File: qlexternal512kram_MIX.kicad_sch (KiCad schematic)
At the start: 13 parts, among them J1 QL_SLOT_DIN41612_CARD, J2 QL_SLOT_DIN41612_CARD, U1 AS6C4008-55PCN, U2 GAL16V8, U3 LM1117-5.0

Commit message: Fix reference for IC
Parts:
- U1: value AS6C4008-55PCN -> HM628512BLFP-7
- U2: value GAL16V8 -> GAL16V8B-25QP
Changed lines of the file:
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@@
     (in_bom yes) (on_board yes)
     (property "Reference" "U1" (id 0) (at 177.165 34.925 0))
-    (property "Value" "AS6C4008-55PCN" (id 1) (at 172.085 37.465 0))
+    (property "Value" "HM628512BLFP-7" (id 1) (at 172.085 37.465 0))
     (property "Footprint" "Package_SO:SSOP-32_11.305x20.495mm_P1.27mm" (id 2) (at 182.88 62.23 0)
       (effects (font (size 1.27 1.27)) hide)
@@
     (in_bom yes) (on_board yes)
     (property "Reference" "U2" (id 0) (at 241.3 106.68 0))
-    (property "Value" "GAL16V8" (id 1) (at 241.3 109.22 0))
+    (property "Value" "GAL16V8B-25QP" (id 1) (at 238.76 109.22 0))
     (property "Footprint" "Package_DIP:DIP-20_W7.62mm_LongPads" (id 2) (at 248.92 125.73 0)
       (effects (font (size 1.27 1.27)) hide)
@@
     )
     (path "/2307b488-4a2e-490d-9ec0-0a3dca2c731a"
-      (reference "U1") (unit 1) (value "AS6C4008-55PCN") (footprint "Package_SO:SSOP-32_11.305x20.495mm_P1.27mm")
+      (reference "U1") (unit 1) (value "HM628512BLFP-7") (footprint "Package_SO:SSOP-32_11.305x20.495mm_P1.27mm")
     )
     (path "/723d583a-7dea-4936-8d46-6a87035bc142"
-      (reference "U2") (unit 1) (value "GAL16V8") (footprint "Package_DIP:DIP-20_W7.62mm_LongPads")
+      (reference "U2") (unit 1) (value "GAL16V8B-25QP") (footprint "Package_DIP:DIP-20_W7.62mm_LongPads")
     )
     (path "/5ac2c658-ce29-46fb-894d-f99c774c93d1"

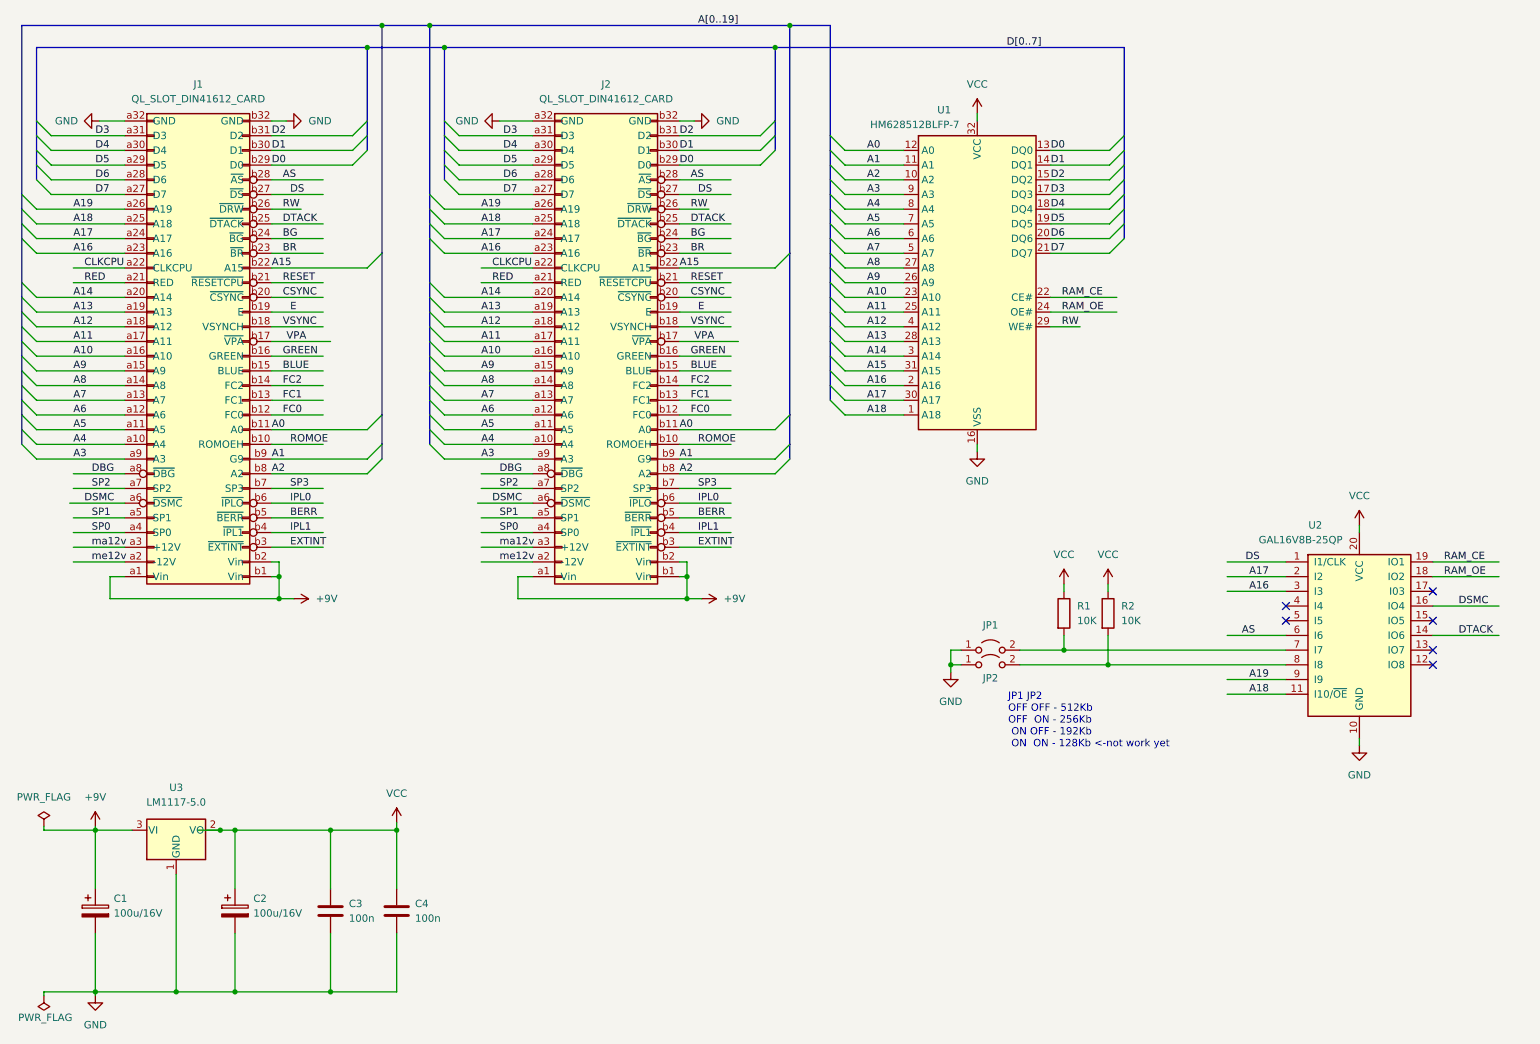
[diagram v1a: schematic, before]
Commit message: Update QL Conector
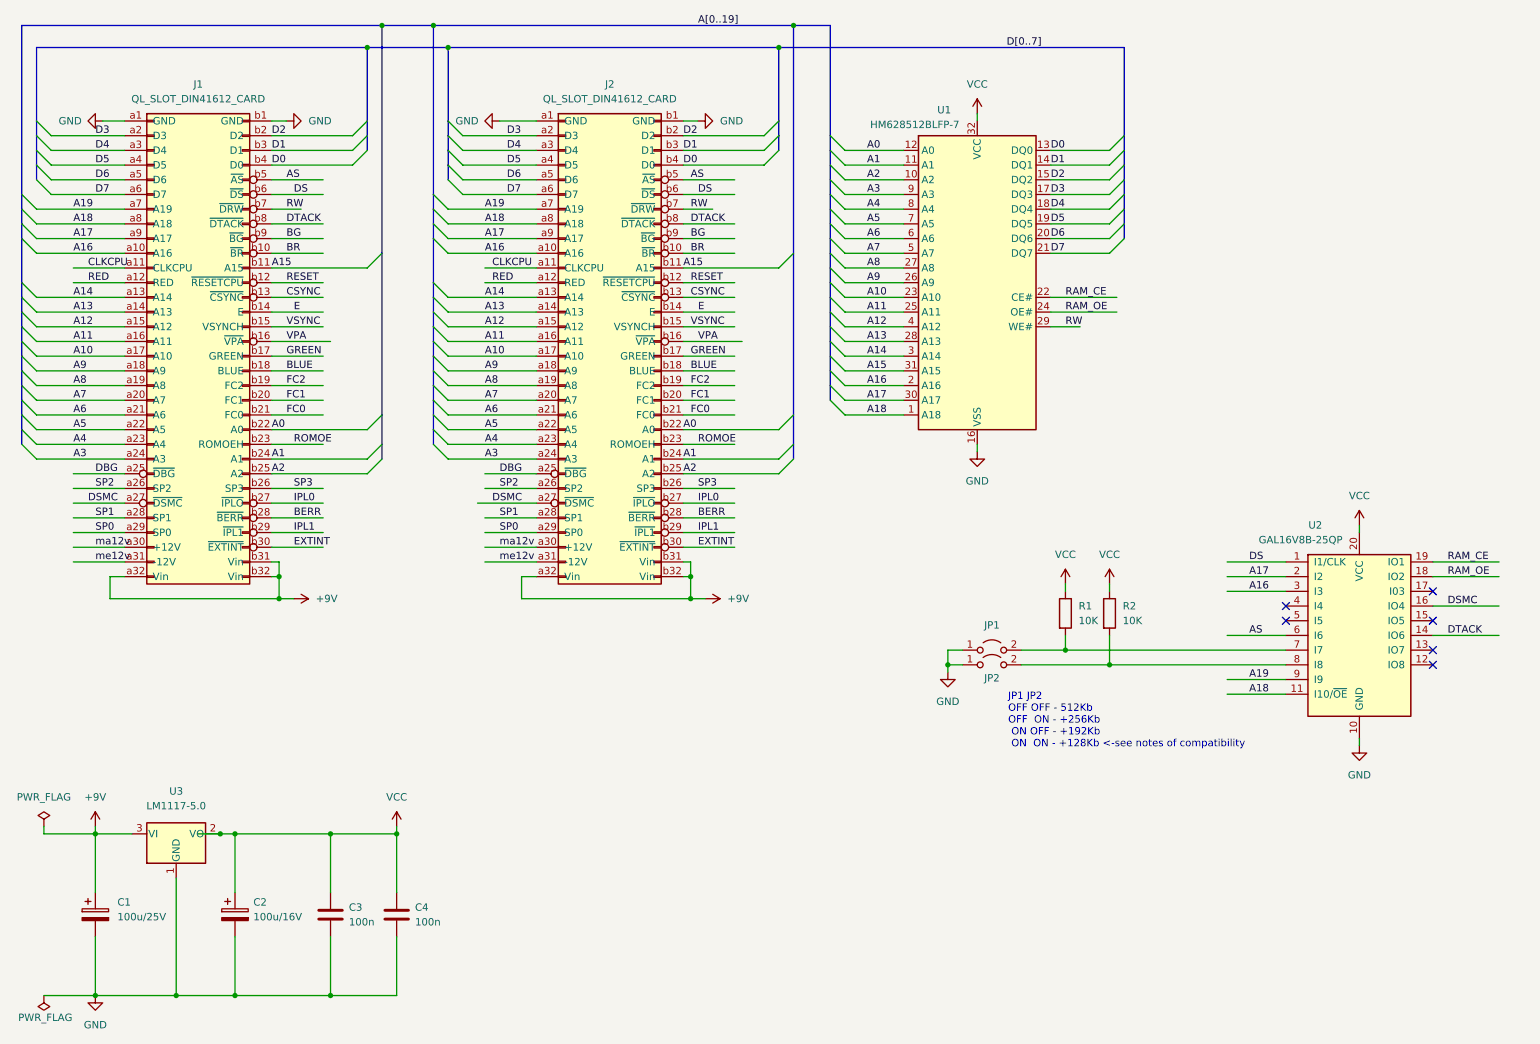
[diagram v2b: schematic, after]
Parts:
- C1: value 100u/16V -> 100u/25V
- J1, J2: symbol 8bits:QL_SLOT_DIN41612_CARD -> 8bits:QL_SLOT_DIN41612
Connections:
- net +9V: now also J1.a32 (Vin), J1.b31 (Vin), J1.b32 (Vin), J2.a32 (Vin), J2.b31 (Vin), J2.b32 (Vin); no longer J1.a1 (Vin), J1.b1 (Vin), J1.b2 (Vin), J2.a1 (Vin), J2.b1 (Vin), J2.b2 (Vin)
- net A0: now also J1.b22 (A0), J2.b22 (A0); no longer J1.b11 (A0), J2.b11 (A0)
- net A1: now also J1.b24 (A1), J2.b24 (A1); no longer J1.b9 (G9), J2.b9 (G9)
- net A10: now also J1.a17 (A10), J2.a17 (A10); no longer J1.a16 (A10), J2.a16 (A10)
- net A11: now also J1.a16 (A11), J2.a16 (A11); no longer J1.a17 (A11), J2.a17 (A11)
- net A12: now also J1.a15 (A12), J2.a15 (A12); no longer J1.a18 (A12), J2.a18 (A12)
- net A13: now also J1.a14 (A13), J2.a14 (A13); no longer J1.a19 (A13), J2.a19 (A13)
- net A14: now also J1.a13 (A14), J2.a13 (A14); no longer J1.a20 (A14), J2.a20 (A14)
- net A15: now also J1.b11 (A15), J2.b11 (A15); no longer J1.b22 (A15), J2.b22 (A15)
- net A16: now also J1.a10 (A16), J2.a10 (A16); no longer J1.a23 (A16), J2.a23 (A16)
- net A17: now also J1.a9 (A17), J2.a9 (A17); no longer J1.a24 (A17), J2.a24 (A17)
- net A18: now also J1.a8 (A18), J2.a8 (A18); no longer J1.a25 (A18), J2.a25 (A18)
- net A19: now also J1.a7 (A19), J2.a7 (A19); no longer J1.a26 (A19), J2.a26 (A19)
- net A2: now also J1.b25 (A2), J2.b25 (A2); no longer J1.b8 (A2), J2.b8 (A2)
- net A3: now also J1.a24 (A3), J2.a24 (A3); no longer J1.a9 (A3), J2.a9 (A3)
- net A4: now also J1.a23 (A4), J2.a23 (A4); no longer J1.a10 (A4), J2.a10 (A4)
- net A5: now also J1.a22 (A5), J2.a22 (A5); no longer J1.a11 (A5), J2.a11 (A5)
- net A6: now also J1.a21 (A6), J2.a21 (A6); no longer J1.a12 (A6), J2.a12 (A6)
- net A7: now also J1.a20 (A7), J2.a20 (A7); no longer J1.a13 (A7), J2.a13 (A7)
- net A8: now also J1.a19 (A8), J2.a19 (A8); no longer J1.a14 (A8), J2.a14 (A8)
- net A9: now also J1.a18 (A9), J2.a18 (A9); no longer J1.a15 (A9), J2.a15 (A9)
- net AS: now also J1.b5 (~{AS}), J2.b5 (~{AS}); no longer J1.b28 (~{AS}), J2.b28 (~{AS})
- net BERR: now also J1.b28 (~{BERR}), J2.b28 (~{BERR}); no longer J1.b5 (~{BERR}), J2.b5 (~{BERR})
- net BG: now also J1.b9 (~{BG}), J2.b9 (~{BG}); no longer J1.b24 (~{BG}), J2.b24 (~{BG})
- net BLUE: now also J1.b18 (BLUE), J2.b18 (BLUE); no longer J1.b15 (BLUE), J2.b15 (BLUE)
- net BR: now also J1.b10 (~{BR}), J2.b10 (~{BR}); no longer J1.b23 (~{BR}), J2.b23 (~{BR})
- net CLKCPU: now also J1.a11 (CLKCPU), J2.a11 (CLKCPU); no longer J1.a22 (CLKCPU), J2.a22 (CLKCPU)
- net CSYNC: now also J1.b13 (~{CSYNC}), J2.b13 (~{CSYNC}); no longer J1.b20 (~{CSYNC}), J2.b20 (~{CSYNC})
- net D0: now also J1.b4 (D0), J2.b4 (D0); no longer J1.b29 (D0), J2.b29 (D0)
- net D1: now also J1.b3 (D1), J2.b3 (D1); no longer J1.b30 (D1), J2.b30 (D1)
- net D2: now also J1.b2 (D2), J2.b2 (D2); no longer J1.b31 (D2), J2.b31 (D2)
- net D3: now also J1.a2 (D3), J2.a2 (D3); no longer J1.a31 (D3), J2.a31 (D3)
- net D4: now also J1.a3 (D4), J2.a3 (D4); no longer J1.a30 (D4), J2.a30 (D4)
- net D5: now also J1.a4 (D5), J2.a4 (D5); no longer J1.a29 (D5), J2.a29 (D5)
- net D6: now also J1.a5 (D6), J2.a5 (D6); no longer J1.a28 (D6), J2.a28 (D6)
- net D7: now also J1.a6 (D7), J2.a6 (D7); no longer J1.a27 (D7), J2.a27 (D7)
- net DBG: now also J1.a25 (~{DBG}), J2.a25 (~{DBG}); no longer J1.a8 (~{DBG}), J2.a8 (~{DBG})
- net DS: now also J1.b6 (~{DS}), J2.b6 (~{DS}); no longer J1.b27 (~{DS}), J2.b27 (~{DS})
- net DSMC: now also J1.a27 (~{DSMC}), J2.a27 (~{DSMC}); no longer J1.a6 (~{DSMC}), J2.a6 (~{DSMC})
- net DTACK: now also J1.b8 (~{DTACK}), J2.b8 (~{DTACK}); no longer J1.b25 (~{DTACK}), J2.b25 (~{DTACK})
- net E: now also J1.b14 (E), J2.b14 (E); no longer J1.b19 (E), J2.b19 (E)
- net EXTINT: now also J1.b30 (~{EXTINT}), J2.b30 (~{EXTINT}); no longer J1.b3 (~{EXTINT}), J2.b3 (~{EXTINT})
- net FC0: now also J1.b21 (FC0), J2.b21 (FC0); no longer J1.b12 (FC0), J2.b12 (FC0)
- net FC1: now also J1.b20 (FC1), J2.b20 (FC1); no longer J1.b13 (FC1), J2.b13 (FC1)
- net FC2: now also J1.b19 (FC2), J2.b19 (FC2); no longer J1.b14 (FC2), J2.b14 (FC2)
- net GND: now also J1.a1 (GND), J1.b1 (GND), J2.a1 (GND), J2.b1 (GND); no longer J1.a32 (GND), J1.b32 (GND), J2.a32 (GND), J2.b32 (GND)
- net GREEN: now also J1.b17 (GREEN), J2.b17 (GREEN); no longer J1.b16 (GREEN), J2.b16 (GREEN)
- net IPL0: now also J1.b27 (~{IPLO}), J2.b27 (~{IPLO}); no longer J1.b6 (~{IPLO}), J2.b6 (~{IPLO})
- net IPL1: now also J1.b29 (~{IPL1}), J2.b29 (~{IPL1}); no longer J1.b4 (~{IPL1}), J2.b4 (~{IPL1})
- net RED: now also J1.a12 (RED), J2.a12 (RED); no longer J1.a21 (RED), J2.a21 (RED)
- net RESET: now also J1.b12 (~{RESETCPU}), J2.b12 (~{RESETCPU}); no longer J1.b21 (~{RESETCPU}), J2.b21 (~{RESETCPU})
- net ROMOE: now also J1.b23 (ROMOEH), J2.b23 (ROMOEH); no longer J1.b10 (ROMOEH), J2.b10 (ROMOEH)
- net RW: now also J1.b7 (~{DRW}), J2.b7 (~{DRW}); no longer J1.b26 (~{DRW}), J2.b26 (~{DRW})
- net SP0: now also J1.a29 (SP0), J2.a29 (SP0); no longer J1.a4 (SP0), J2.a4 (SP0)
- net SP1: now also J1.a28 (SP1), J2.a28 (SP1); no longer J1.a5 (SP1), J2.a5 (SP1)
- net SP2: now also J1.a26 (SP2), J2.a26 (SP2); no longer J1.a7 (SP2), J2.a7 (SP2)
- net SP3: now also J1.b26 (SP3), J2.b26 (SP3); no longer J1.b7 (SP3), J2.b7 (SP3)
- net VPA: now also J1.b16 (~{VPA}), J2.b16 (~{VPA}); no longer J1.b17 (~{VPA}), J2.b17 (~{VPA})
- net VSYNC: now also J1.b15 (VSYNCH), J2.b15 (VSYNCH); no longer J1.b18 (VSYNCH), J2.b18 (VSYNCH)
- net ma12v: now also J1.a30 (+12V), J2.a30 (+12V); no longer J1.a3 (+12V), J2.a3 (+12V)
- net me12v: now also J1.a31 (-12V), J2.a31 (-12V); no longer J1.a2 (-12V), J2.a2 (-12V)
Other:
- note added: "JP1 JP2 OFF OFF - 512Kb OFF ON - +256Kb ON OFF - +192Kb ON ON - +128Kb <-see notes of compatibility"
- note removed: "JP1 JP2 OFF OFF - 512Kb OFF ON - 256Kb ON OFF - 192Kb ON ON - 128Kb <-not work yet"
- moved on the sheet: C1, C2, C3, C4, J2, U3

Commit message: Add compatibility with MiniTrump Card, and moved GAL to galasm
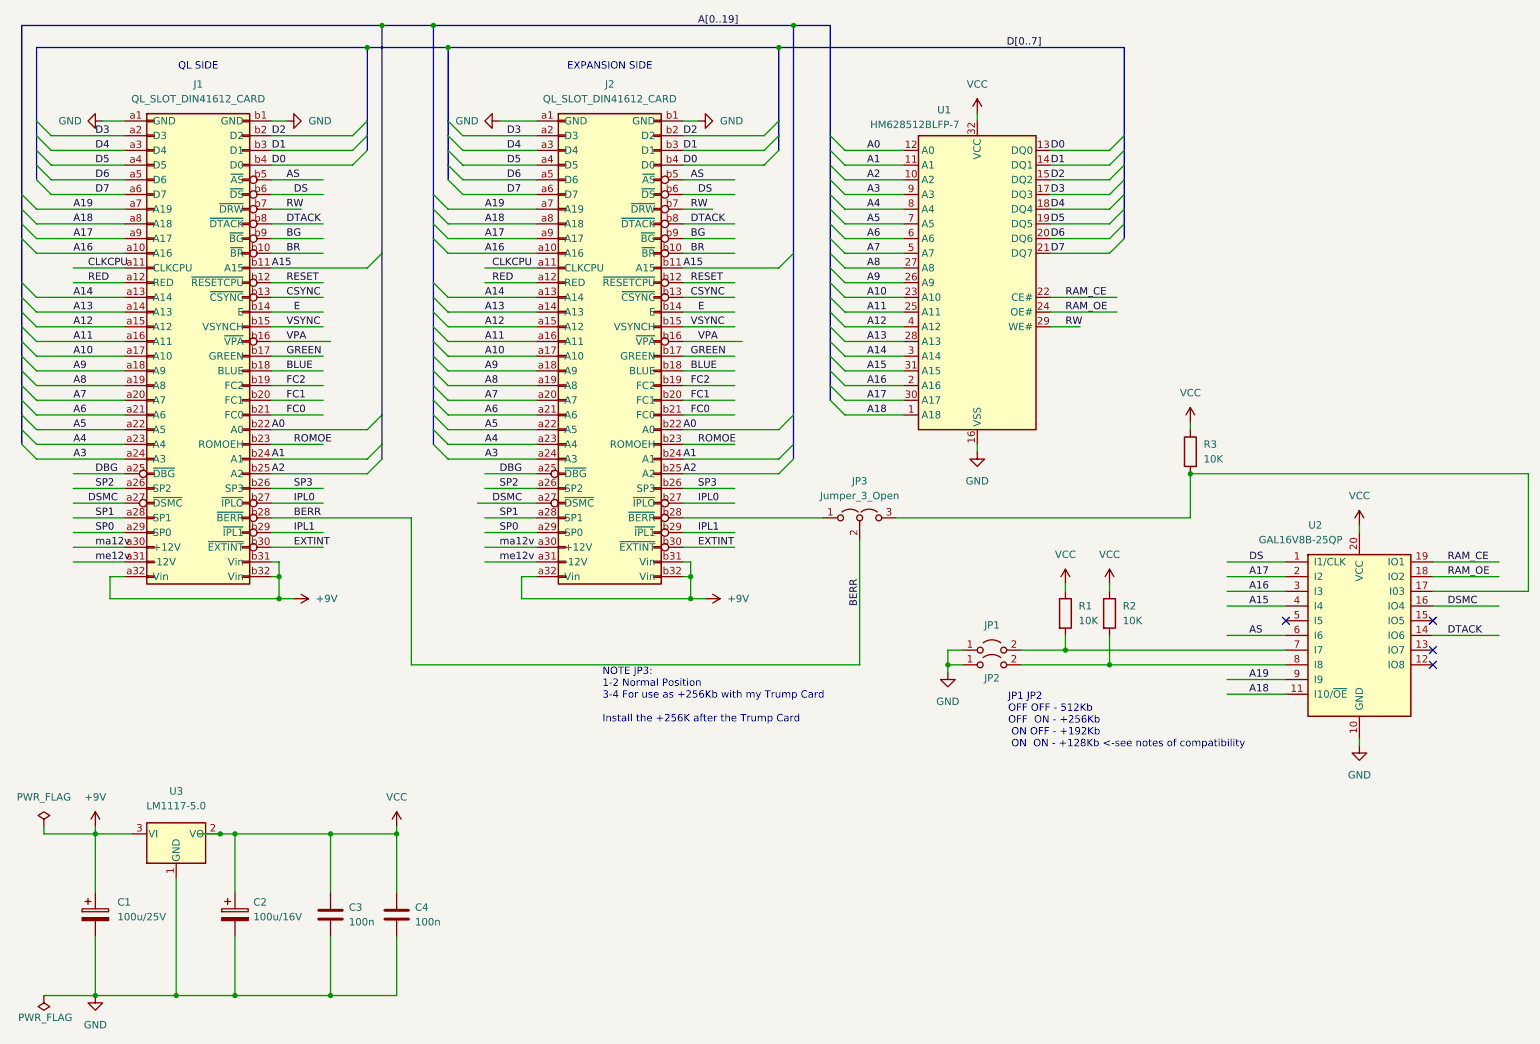
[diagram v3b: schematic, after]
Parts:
- added JP3: Jumper_3_Open, Jumper:SolderJumper-3_P1.3mm_Open_Pad1.0x1.5mm, symbol Jumper:Jumper_3_Open
- added R3: 10K, Resistor_SMD:R_1206_3216Metric_Pad1.30x1.75mm_HandSolder, symbol Device:R
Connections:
- net A15: now also U2.4 (I4)
- net BERR: now also JP3.2 (C); no longer J2.b28 (~{BERR})
- net VCC: now also R3.1
- net at U2.17 (I03): now also JP3.3 (B), R3.2
- new net: J2.b28 (~{BERR}), JP3.1 (A)
- no-connect marks 6 -> 4
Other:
- note added: "EXPANSION SIDE"
- note added: "NOTE JP3: 1-2 Normal Position 3-4 For use as +256Kb with my Trump Card Install the +256K after the Trump Card"
- note added: "QL SIDE"

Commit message: minor typos
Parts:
- J1: value QL_SLOT_DIN41612_CARD -> QL_SLOT_DIN41612_FEMALE-90degrees
- J2: value QL_SLOT_DIN41612_CARD -> QL_SLOT_DIN41612_MALE_90degrees
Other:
- note added: "EXPANSION SIDE (M)"
- note added: "NOTE JP3: 1-2 Normal Position 2-3 For use as +256Kb with my Trump Card Install the +256K after the Trump Card"
- note added: "QL SIDE (F)"
- note removed: "EXPANSION SIDE"
- note removed: "NOTE JP3: 1-2 Normal Position 3-4 For use as +256Kb with my Trump Card Install the +256K after the Trump Card"
- note removed: "QL SIDE"
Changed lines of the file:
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@@
 	(title_block
 		(title "External Expansion 512Kb memory for Sinclair QL")
-		(date "2024-11-08")
+		(date "2024-11-22")
 		(rev "3")
 		(company "(C) 2022 Alvaro Alea Fdz")
@@
 		)
 	)
-	(text "NOTE JP3:\n1-2 Normal Position \n3-4 For use as +256Kb with my Trump Card\n\nInstall the +256K after the Trump Card \n"
+	(text "NOTE JP3:\n1-2 Normal Position \n2-3 For use as +256Kb with my Trump Card\n\nInstall the +256K after the Trump Card \n"
 		(exclude_from_sim no)
 		(at 118.11 136.144 0)
@@
 		)
 	)
-	(text "EXPANSION SIDE"
+	(text "EXPANSION SIDE (M)"
 		(exclude_from_sim no)
 		(at 119.38 27.432 0)
@@
 		)
 	)
-	(text "QL SIDE"
+	(text "QL SIDE (F)"
 		(exclude_from_sim no)
 		(at 48.26 27.432 0)
@@
 			)
 		)
-		(property "Value" "QL_SLOT_DIN41612_CARD"
+		(property "Value" "QL_SLOT_DIN41612_MALE_90degrees"
 			(at 119.38 33.02 0)
 			(effects
@@
 			)
 		)
-		(property "Value" "QL_SLOT_DIN41612_CARD"
+		(property "Value" "QL_SLOT_DIN41612_FEMALE-90degrees"
 			(at 48.26 33.02 0)
 			(effects
